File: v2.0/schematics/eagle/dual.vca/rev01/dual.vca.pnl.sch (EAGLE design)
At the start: 30 parts, among them J1 CV1, J10 CV4, J11 IN4, J12 OUT4, J2 IN1, J3 OUT1, J4 CV2, J5 IN2, J6 OUT2, J7 CV3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

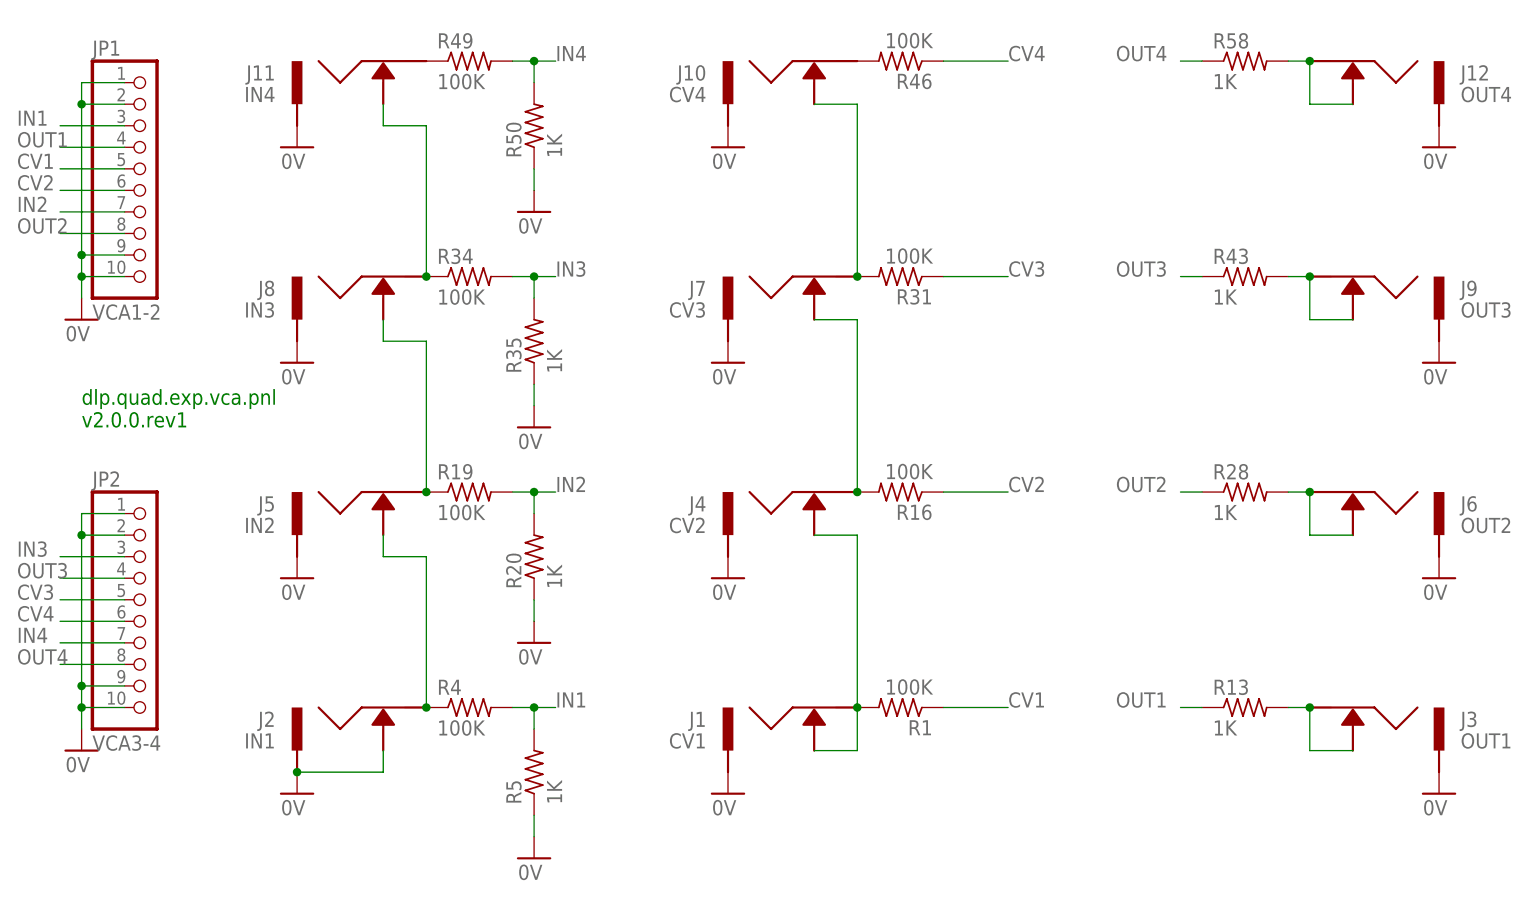
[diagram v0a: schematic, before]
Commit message: Added cam files; annotate panel schem with board edits; update cv resistor values
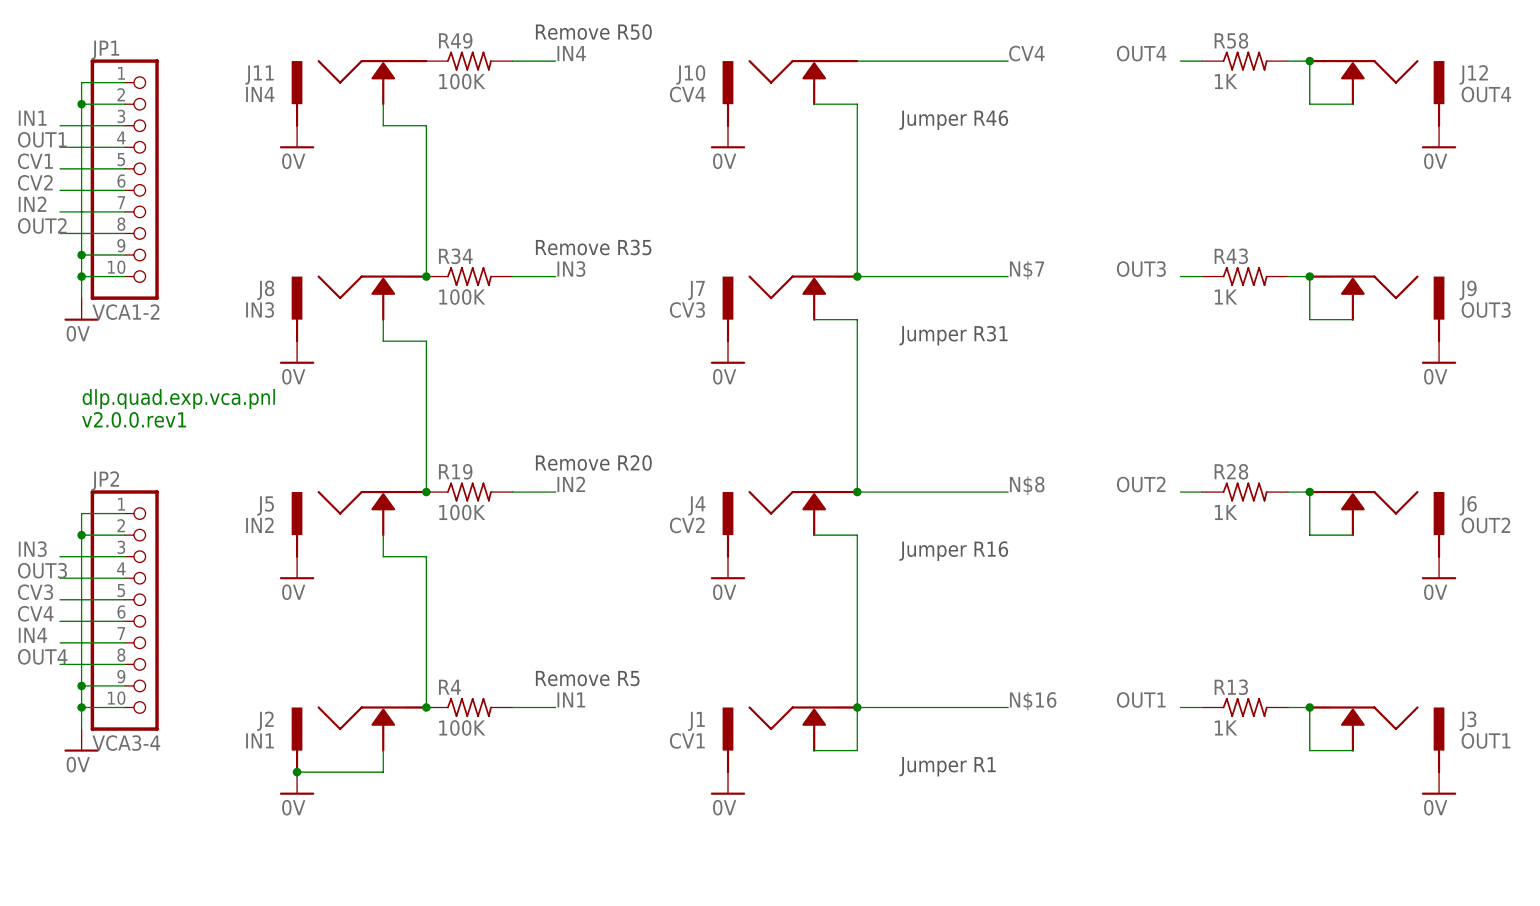
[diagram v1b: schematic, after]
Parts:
- removed R1, R16, R31, R46: 100K, resistor:R-US_0207/7
- removed R20, R35, R5, R50: 1K, resistor:R-US_0207/7
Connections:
- removed net N$6: J10.P$2, R46.2
- net 0V: no longer R20.1, R35.1, R5.1, R50.1
- net CV1: no longer R1.1
- net CV2: no longer R16.1
- net CV3: no longer R31.1
- net CV4: now also J10.P$2; no longer R46.1
- net IN1: no longer R5.2
- net IN2: no longer R20.2
- net IN3: no longer R35.2
- net IN4: no longer R50.2
- net N$16: no longer R1.2
- net N$7: no longer R31.2
- net N$8: no longer R16.2
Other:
- note added: "Jumper R1"
- note added: "Jumper R16"
- note added: "Jumper R31"
- note added: "Jumper R46"
- note added: "Remove R20"
- note added: "Remove R35"
- note added: "Remove R5"
- note added: "Remove R50"
